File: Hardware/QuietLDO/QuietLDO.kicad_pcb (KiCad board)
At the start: 2 copper layers, 95 parts

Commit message: start QuietPCB
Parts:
- added hole1: ~, persional_library:m3 125x300, F.Cu at (211.5, 105.5)
- added hole2: ~, persional_library:m3 125x300, F.Cu at (211.5, 65.5)
- added hole3: ~, persional_library:m3 125x300, F.Cu at (121.5, 65.5)
- added hole4: ~, persional_library:m3 125x300, F.Cu at (121.5, 105.5)
- C1, C10, C11, C12, C13, C14, C15, C16, C17, C18, C19, C2, C20, C21, C22, C23, C24, C25, C26, C27, C28, C29, C3, C30, C31, C32, C37, C4, C5, C6, C7, C8, C9: footprint persional_library:C0805 -> persional_library:C0603
- CN10, CN13, CN15, CN16, CN3, CN4, CN7, CN8: moved to B.Cu
- moved CN2 188.2 mm to (193.6, 107.0)
- moved CN8 182.9 mm to (200.4, 107.0), turned to 180 degrees
- moved CN12 176.4 mm to (200.4, 107.0)
- moved CN1 173.0 mm to (173.1, 107.0)
- moved C29 166.7 mm to (199.4, 101.8), turned to -90 degrees
- moved CN16 163.6 mm to (193.6, 107.0), turned to 180 degrees
- moved C31 163.1 mm to (197.6, 101.8), turned to -90 degrees
- moved C27 162.2 mm to (194.1, 101.8), turned to -90 degrees
- moved CN7 160.6 mm to (173.1, 107.0), turned to 180 degrees
- moved C32 160.6 mm to (195.9, 101.8), turned to -90 degrees
- moved CN11 160.5 mm to (180.0, 107.0)
- moved SW2 160.5 mm to (204.4, 94.3), turned to 90 degrees
- moved C28 159.7 mm to (192.3, 101.8), turned to -90 degrees
- moved C26 159.3 mm to (192.9, 91.0), turned to 90 degrees
- moved C37 158.8 mm to (204.9, 68.2), turned to 180 degrees
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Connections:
- CN10 pad 1: +3V3 -> GND
- CN10 pad 2: GND -> +3V3
- CN13 pad 1: +5V -> GND
- CN13 pad 2: GND -> +5V
- CN15 pad 1: +1V8 -> GND
- CN15 pad 2: GND -> +1V8
- CN16 pad 1: VDD -> GND
- CN16 pad 2: GND -> VDD
- CN3 pad 1: +5V -> GND
- CN3 pad 2: GND -> +5V
- CN4 pad 1: +3V3 -> GND
- CN4 pad 2: GND -> +3V3
- CN7 pad 1: +1V8 -> GND
- CN7 pad 2: GND -> +1V8
- CN8 pad 1: VDD -> GND
- CN8 pad 2: GND -> VDD
- SW1 pad 1: VIN -> unconnected-(SW1-Pad1)
- SW1 pad 3: unconnected-(SW1-Pad3) -> VIN
- U2 pad 20: +5V -> +3V3
- U3 pad 20: +5V -> +1V8
- U4 pad 20: +5V -> VDD
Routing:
- net VDD: track 0.00 -> 22.0 mm
- net +1V8: track 0.00 -> 19.3 mm
- net +3V3: track 0.00 -> 18.9 mm
- net +5V: track 0.00 -> 18.6 mm
- net VCC: track 0.00 -> 7.38 mm
- net Net-(U1-0P8V): track 0.00 -> 6.98 mm
- net VDC: track 0.00 -> 6.84 mm
- net Net-(U1-6P4V2): track 0.00 -> 6.29 mm
- net Net-(U1-6P4V1): track 0.00 -> 6.16 mm
- net Net-(U1-0P4V): track 0.00 -> 4.60 mm
- net Net-(U1-3P2V): track 0.00 -> 3.89 mm
- net Net-(U1-1P6V): track 0.00 -> 3.85 mm
- net Net-(U1-0P2V): track 0.00 -> 3.36 mm
- net Net-(U5-SW): track 0.00 -> 2.92 mm
- net Net-(U1-0P1V): track 0.00 -> 2.45 mm
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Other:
- board outline added: 100 x 50 mm

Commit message: add QuietLDO PCB
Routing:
- net VCC: track 7.38 -> 162.2 mm, vias 0 -> 8
- net VDC: track 6.84 -> 56.0 mm
- net VIN: track 0.00 -> 44.7 mm
- net Net-(U5-EN): track 0.00 -> 13.0 mm, vias 0 -> 2
- net +5V: track 18.6 -> 31.5 mm, vias 0 -> 2
- net +3V3: track 18.9 -> 31.8 mm, vias 0 -> 2
- net VDD: track 22.0 -> 34.5 mm, vias 0 -> 2
- net +1V8: track 19.3 -> 31.4 mm, vias 0 -> 2
- net Net-(U5-SW): track 2.92 -> 12.4 mm
- net Net-(U4-0P1V): track 0.00 -> 8.16 mm
- net Net-(U2-0P8V): track 0.00 -> 7.29 mm
- net Net-(SW2-PIN9): track 0.00 -> 7.22 mm
- net Net-(U3-0P8V): track 0.00 -> 6.97 mm
- net Net-(SW2-PIN10): track 0.00 -> 6.89 mm
- net Net-(U2-6P4V2): track 0.00 -> 6.61 mm
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- added copper zone on F.Cu, net +1V8
- added copper zone on F.Cu, net +3V3
- added copper zone on F.Cu, net +5V
- added copper zone on B.Cu, net GND
- added copper zone on F.Cu, net GND
- added copper zone on F.Cu, net Net-(U5-SW)
- added copper zone on F.Cu, net VCC
- added copper zone on F.Cu, net VDC
- added copper zone on F.Cu, net VDD
- added copper zone on F.Cu, net VIN

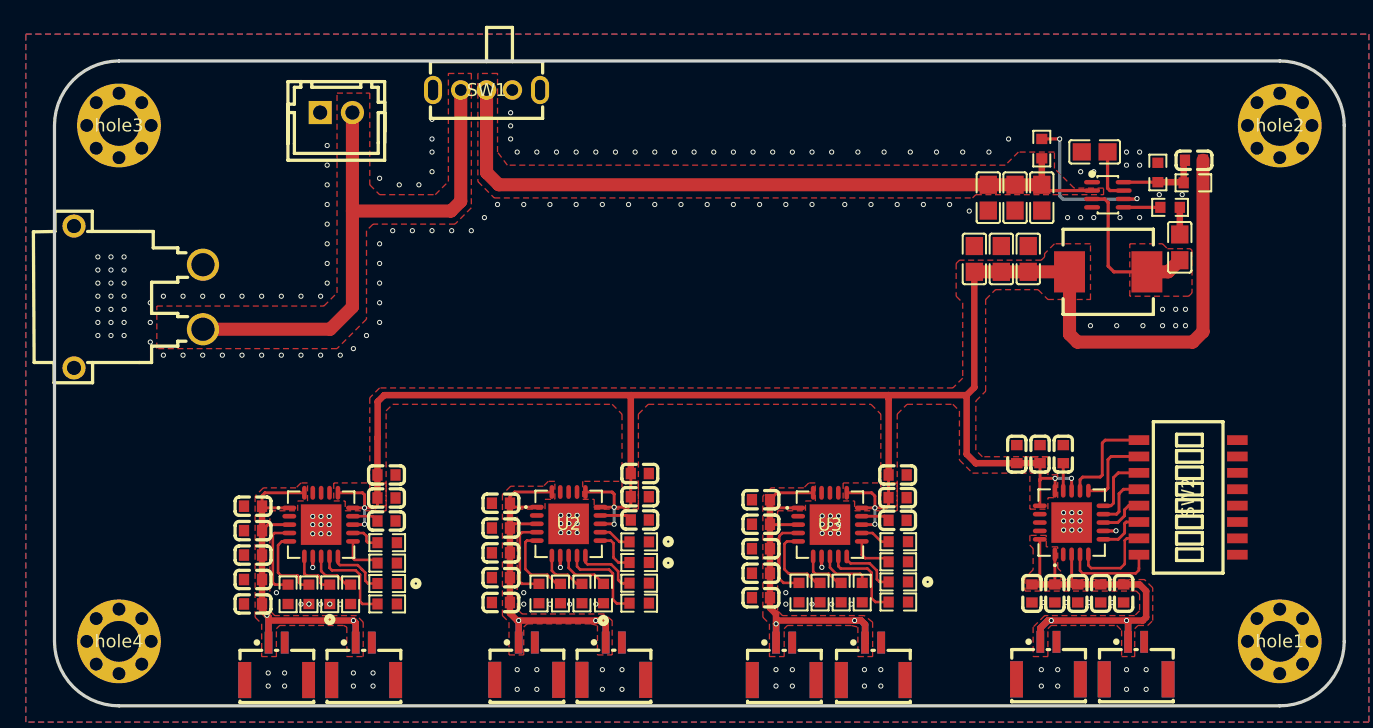
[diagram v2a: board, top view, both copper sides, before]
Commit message: complete QuietLDO
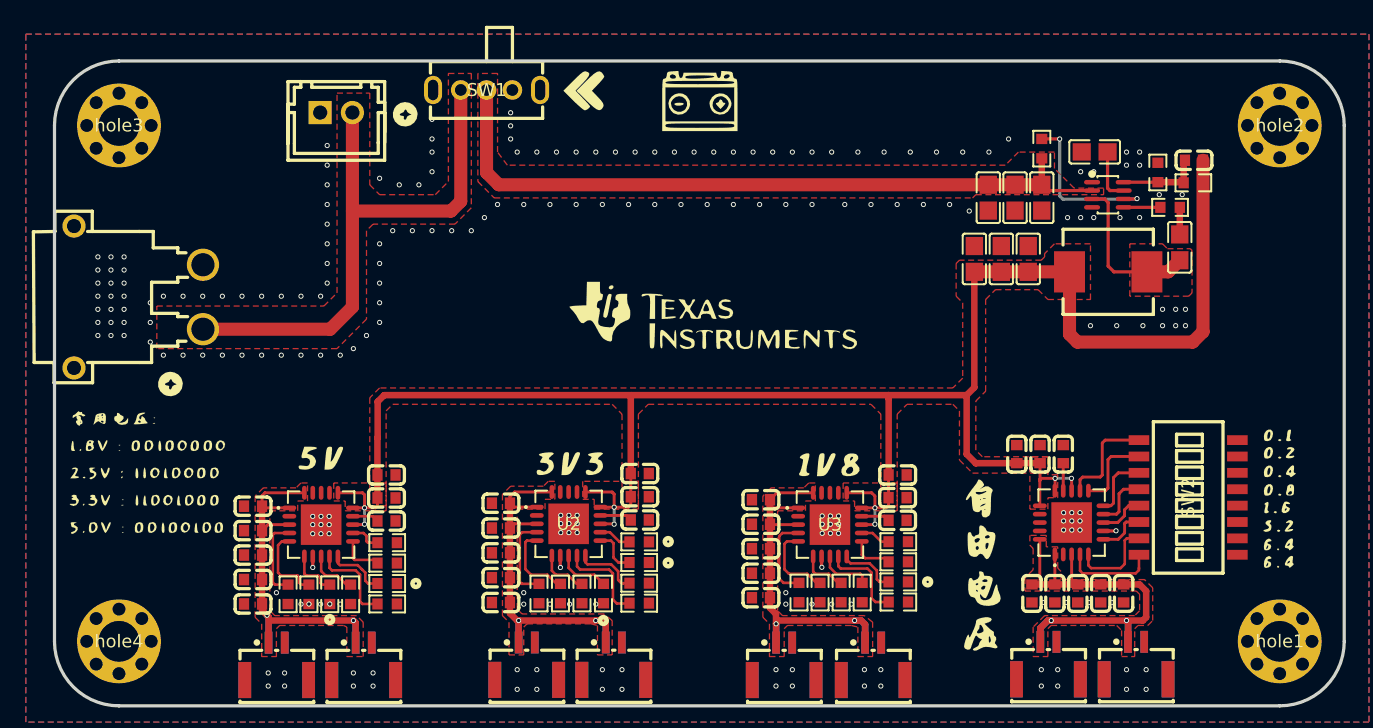
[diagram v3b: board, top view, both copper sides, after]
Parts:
- added G***: LOGO, logo:DownSilkscreen, F.Cu at (158.6, 85.3)
- added G***: LOGO, logo:UpSilkscreen, F.Cu at (166.5, 85.5)

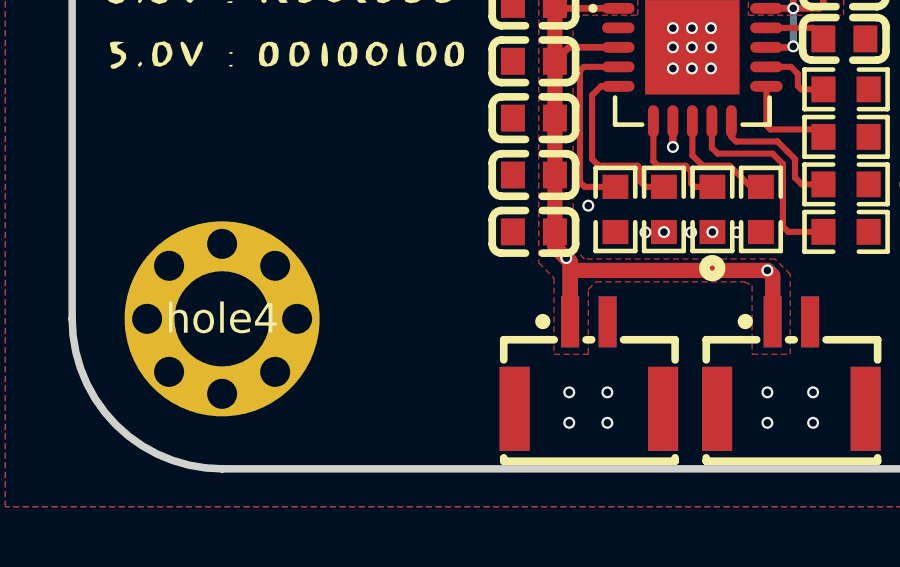
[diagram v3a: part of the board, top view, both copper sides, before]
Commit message: complete the datasheet of QuietLDO
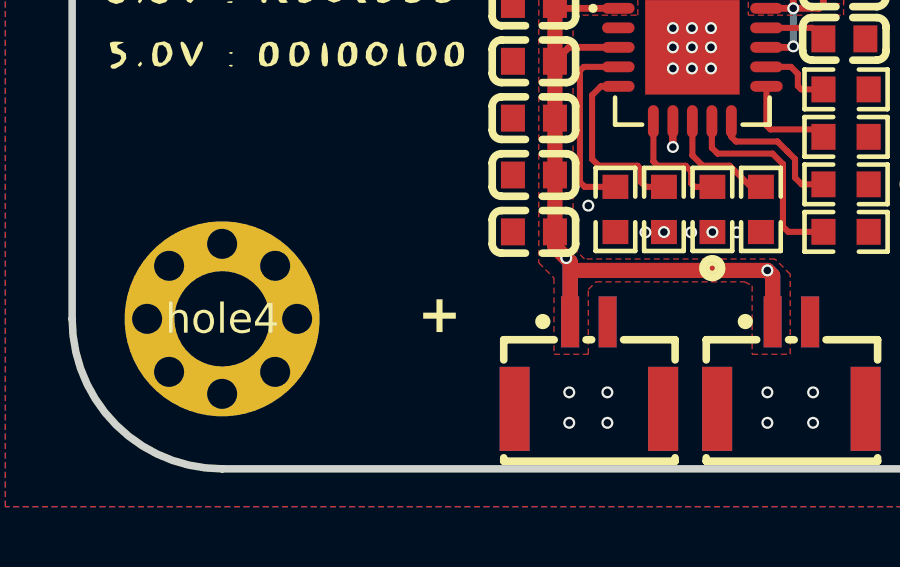
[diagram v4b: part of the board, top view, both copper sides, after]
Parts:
- removed the G*** at (158.6, 85.3)
- added G***: LOGO, logo:Down_logo_2, F.Cu at (158.7, 85.5)
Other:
- board text added: "+"

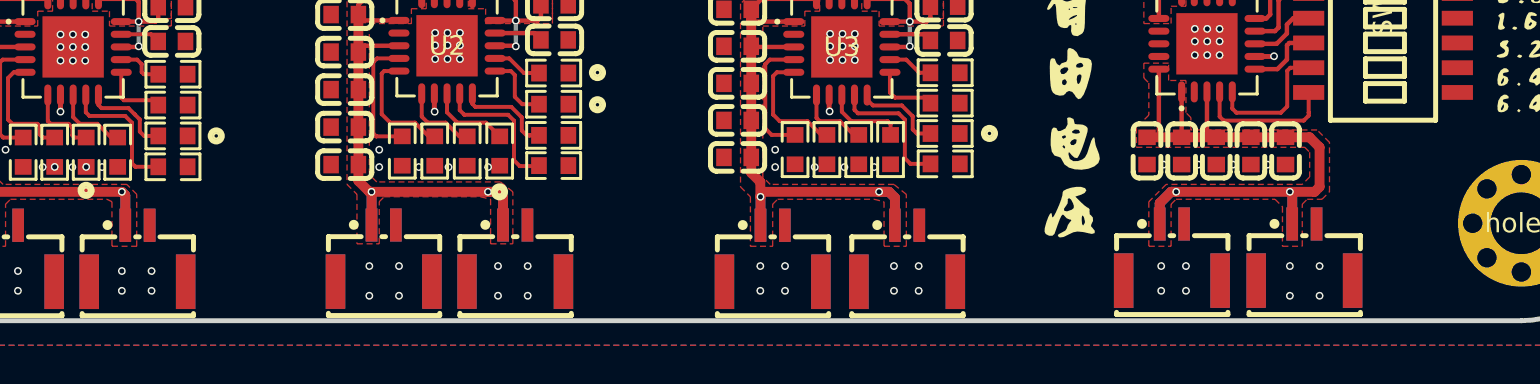
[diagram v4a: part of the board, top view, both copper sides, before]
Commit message: add BOM Checklist Function
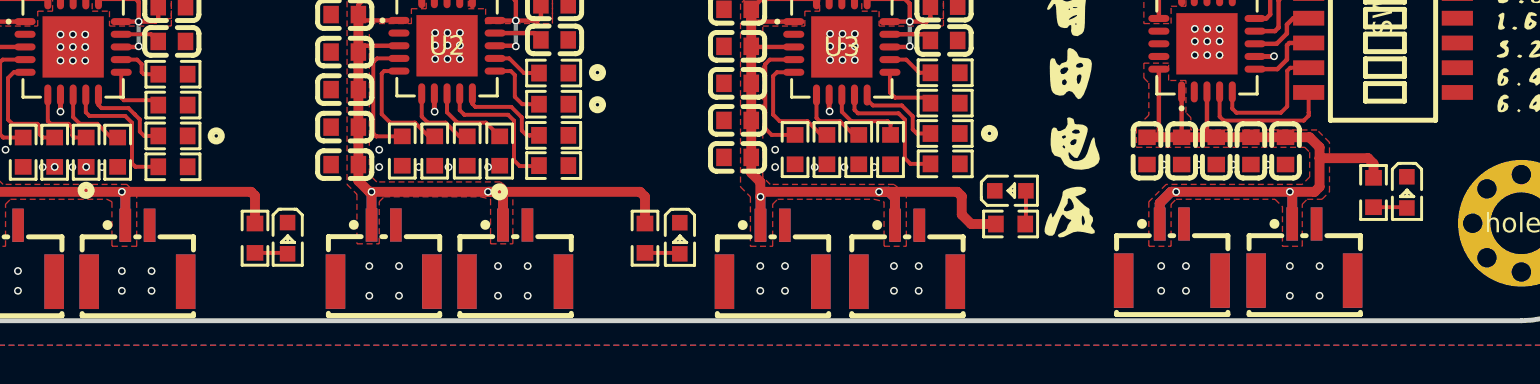
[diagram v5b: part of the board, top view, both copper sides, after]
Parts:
- added LED1: ~, persional_library:LED0603-RD, F.Cu at (205.6, 103.9)
- added LED2: ~, persional_library:LED0603-RD, F.Cu at (185.3, 103.8)
- added LED3: ~, persional_library:LED0603-RD, F.Cu at (168.3, 106.3)
- added LED4: ~, persional_library:LED0603-RD, F.Cu at (148.2, 106.3)
- added R25: 10kΩ, persional_library:R0603, F.Cu at (203.9, 103.9)
- added R26: 10kΩ, persional_library:R0603, F.Cu at (185.3, 105.5)
- added R27: 10kΩ, persional_library:R0603, F.Cu at (166.5, 106.3)
- added R28: 10kΩ, persional_library:R0603, F.Cu at (146.5, 106.3)
- R1, R11, R12, R14, R15, R16, R17, R18, R2, R20, R21, R22, R23, R24, R4, R5, R7, R8: value 0Ω -> NC
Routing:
- net +3V3: track 31.8 -> 41.3 mm
- net +5V: track 31.5 -> 39.8 mm
- net +1V8: track 31.4 -> 38.4 mm
- net VDD: track 34.5 -> 38.1 mm
- net Net-(LED3-+): track 0.00 -> 1.81 mm
- net Net-(LED1-+): track 0.00 -> 1.73 mm
- net Net-(LED2-+): track 0.00 -> 1.72 mm
- net Net-(LED4-+): track 0.00 -> 1.69 mm
